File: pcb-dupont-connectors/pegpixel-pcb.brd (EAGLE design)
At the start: 22.6 x 14.2 mm, 6 parts

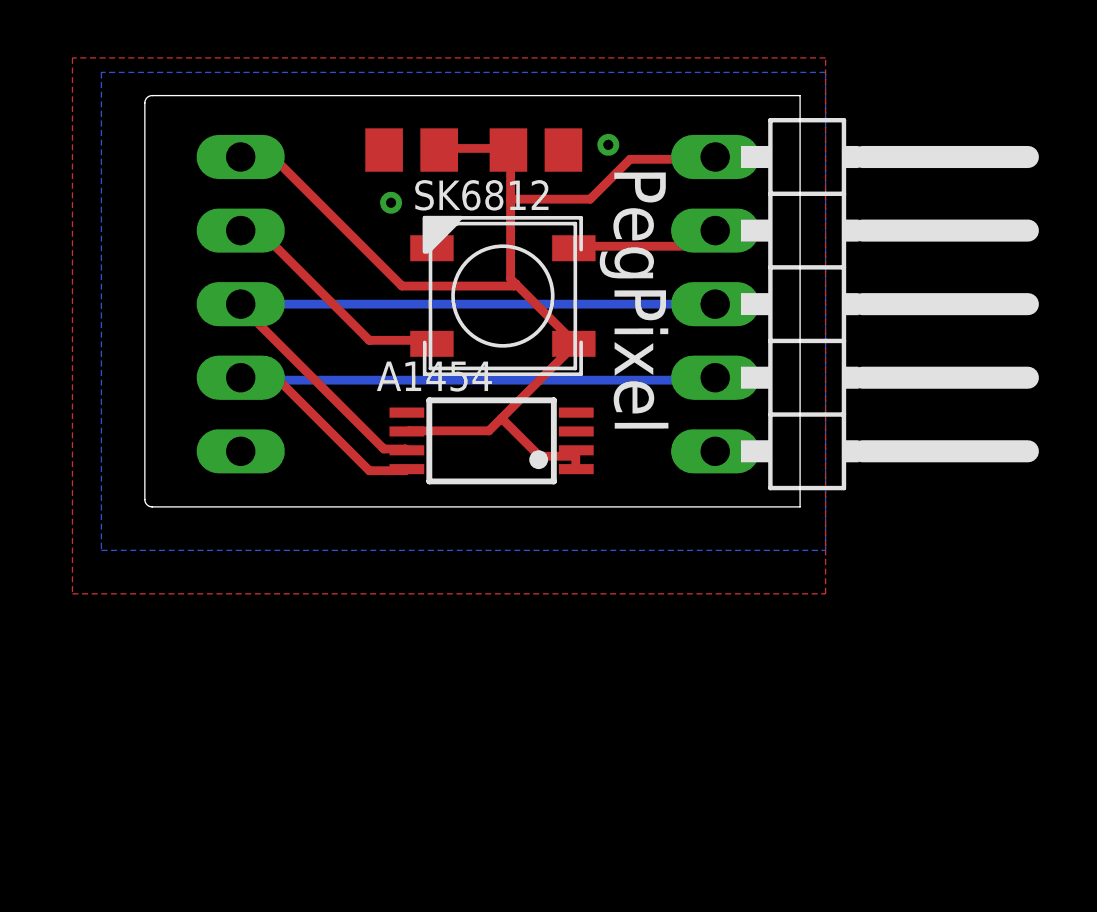
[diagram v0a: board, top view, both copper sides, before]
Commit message: Remove second capacitor
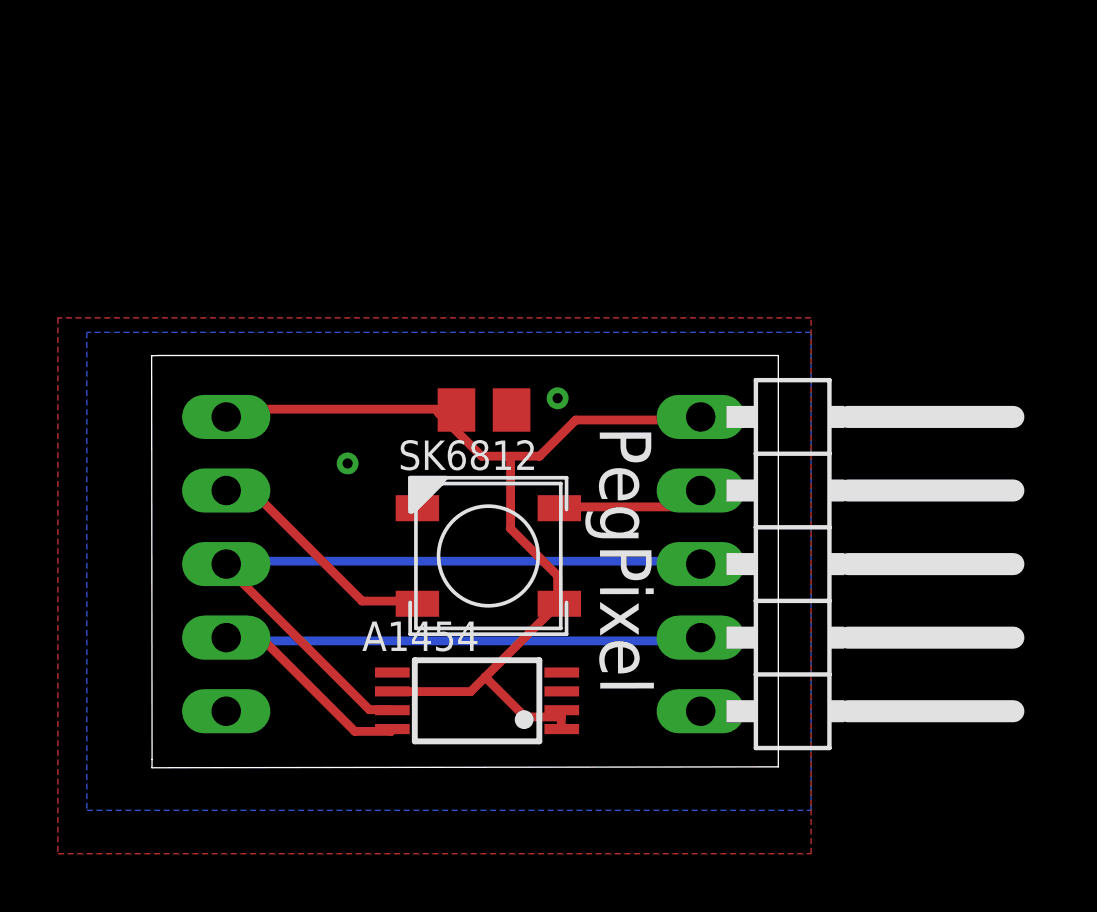
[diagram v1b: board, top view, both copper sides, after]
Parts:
- removed C2: 104, rcl:C0805
- moved C1 9.32 mm to (12.2, 12.3), turned to 0 degrees
- moved JP1 8.99 mm to (-0.50, 7.03)
- moved JP2 8.99 mm to (23.5, 7.03)
- moved LED1 8.99 mm to (12.4, 7.31)
- moved H1 8.99 mm to (12.0, 2.31)
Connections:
- net GND: no longer C2.2
- net VCC: no longer C2.1
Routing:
- net VCC: track 40.0 -> 35.6 mm
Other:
- board size 22.6 x 14.2 mm -> 21.6 x 14.2 mm
